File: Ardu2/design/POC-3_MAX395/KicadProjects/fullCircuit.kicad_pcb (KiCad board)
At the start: 2 copper layers, 179.3 x 143.5 mm, 132 parts, among them P1 CONN_01X02, P2 CONN_01X14, P3 CONN_01X14, P4 CONN_01X01, P7 CONN_01X15, U1 Pyboard, U10 MAX395, U11 MAX395, U12 MAX395, U13 MAX395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

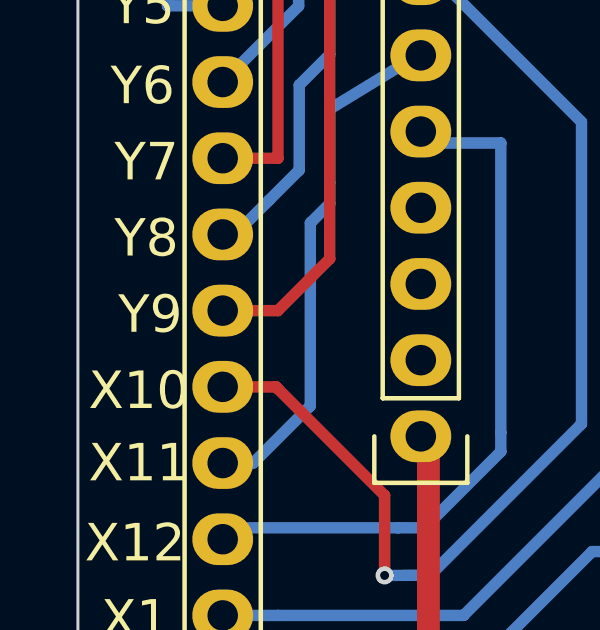
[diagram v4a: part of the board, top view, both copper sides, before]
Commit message: reorginized directories
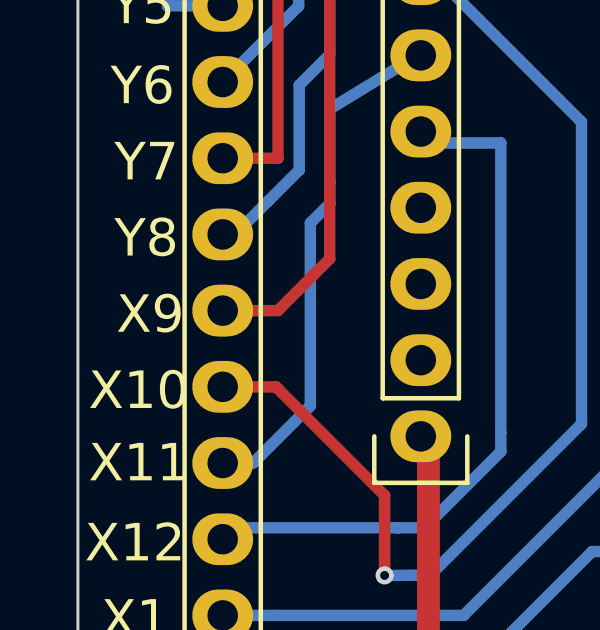
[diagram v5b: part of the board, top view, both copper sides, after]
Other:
- board text added: "X9"
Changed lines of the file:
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@@
-(kicad_pcb (version 4) (host pcbnew 0.201511031201+6292~30~ubuntu15.04.1-product)
+(kicad_pcb (version 4) (host pcbnew 4.1.0-alpha+201606081202+6904~45~ubuntu15.10.1-product)
   (general
     (links 508)
@@
       (hpglpenspeed 20)
       (hpglpendiameter 15)
-      (hpglpenoverlay 2)
       (psnegative false)
       (psa4output false)
@@
       (effects (font (size 1 1) (thickness 0.15)))
     )
-    (fp_text value HEATSINK (at 12.065 8.255 360) (layer F.Fab)
+    (fp_text value HEATSINK (at 12.065 8.255) (layer F.Fab)
       (effects (font (size 1 1) (thickness 0.15)))
     )
@@
     (at 107.95 135.89 270)
     (descr "<b>TO-220</b><p> 5 lead, National Semiconductor T05D")
-    (fp_text reference U2 (at 4.445 1.27 360) (layer F.SilkS)
+    (fp_text reference U2 (at 4.445 1.27) (layer F.SilkS)
       (effects (font (size 1.6891 1.6891) (thickness 0.1778)) (justify left bottom))
     )
-    (fp_text value LM2596 (at 7.62 5.715 360) (layer F.SilkS)
+    (fp_text value LM2596 (at 7.62 5.715) (layer F.SilkS)
       (effects (font (size 1.6891 1.6891) (thickness 0.1778)) (justify left bottom))
     )
@@
     (effects (font (size 1.25 1.25) (thickness 0.2)))
   )
-  (gr_text Y9 (at 64.643 93.599) (layer F.SilkS)
+  (gr_text X9 (at 64.643 93.599) (layer F.SilkS)
     (effects (font (size 1.25 1.25) (thickness 0.2)))
   )
